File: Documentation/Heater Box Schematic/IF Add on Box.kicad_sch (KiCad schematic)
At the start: 21 parts, among them J1 DB37 Female, J2 DB37 Male, K1 Heater Relay, M1 Fan

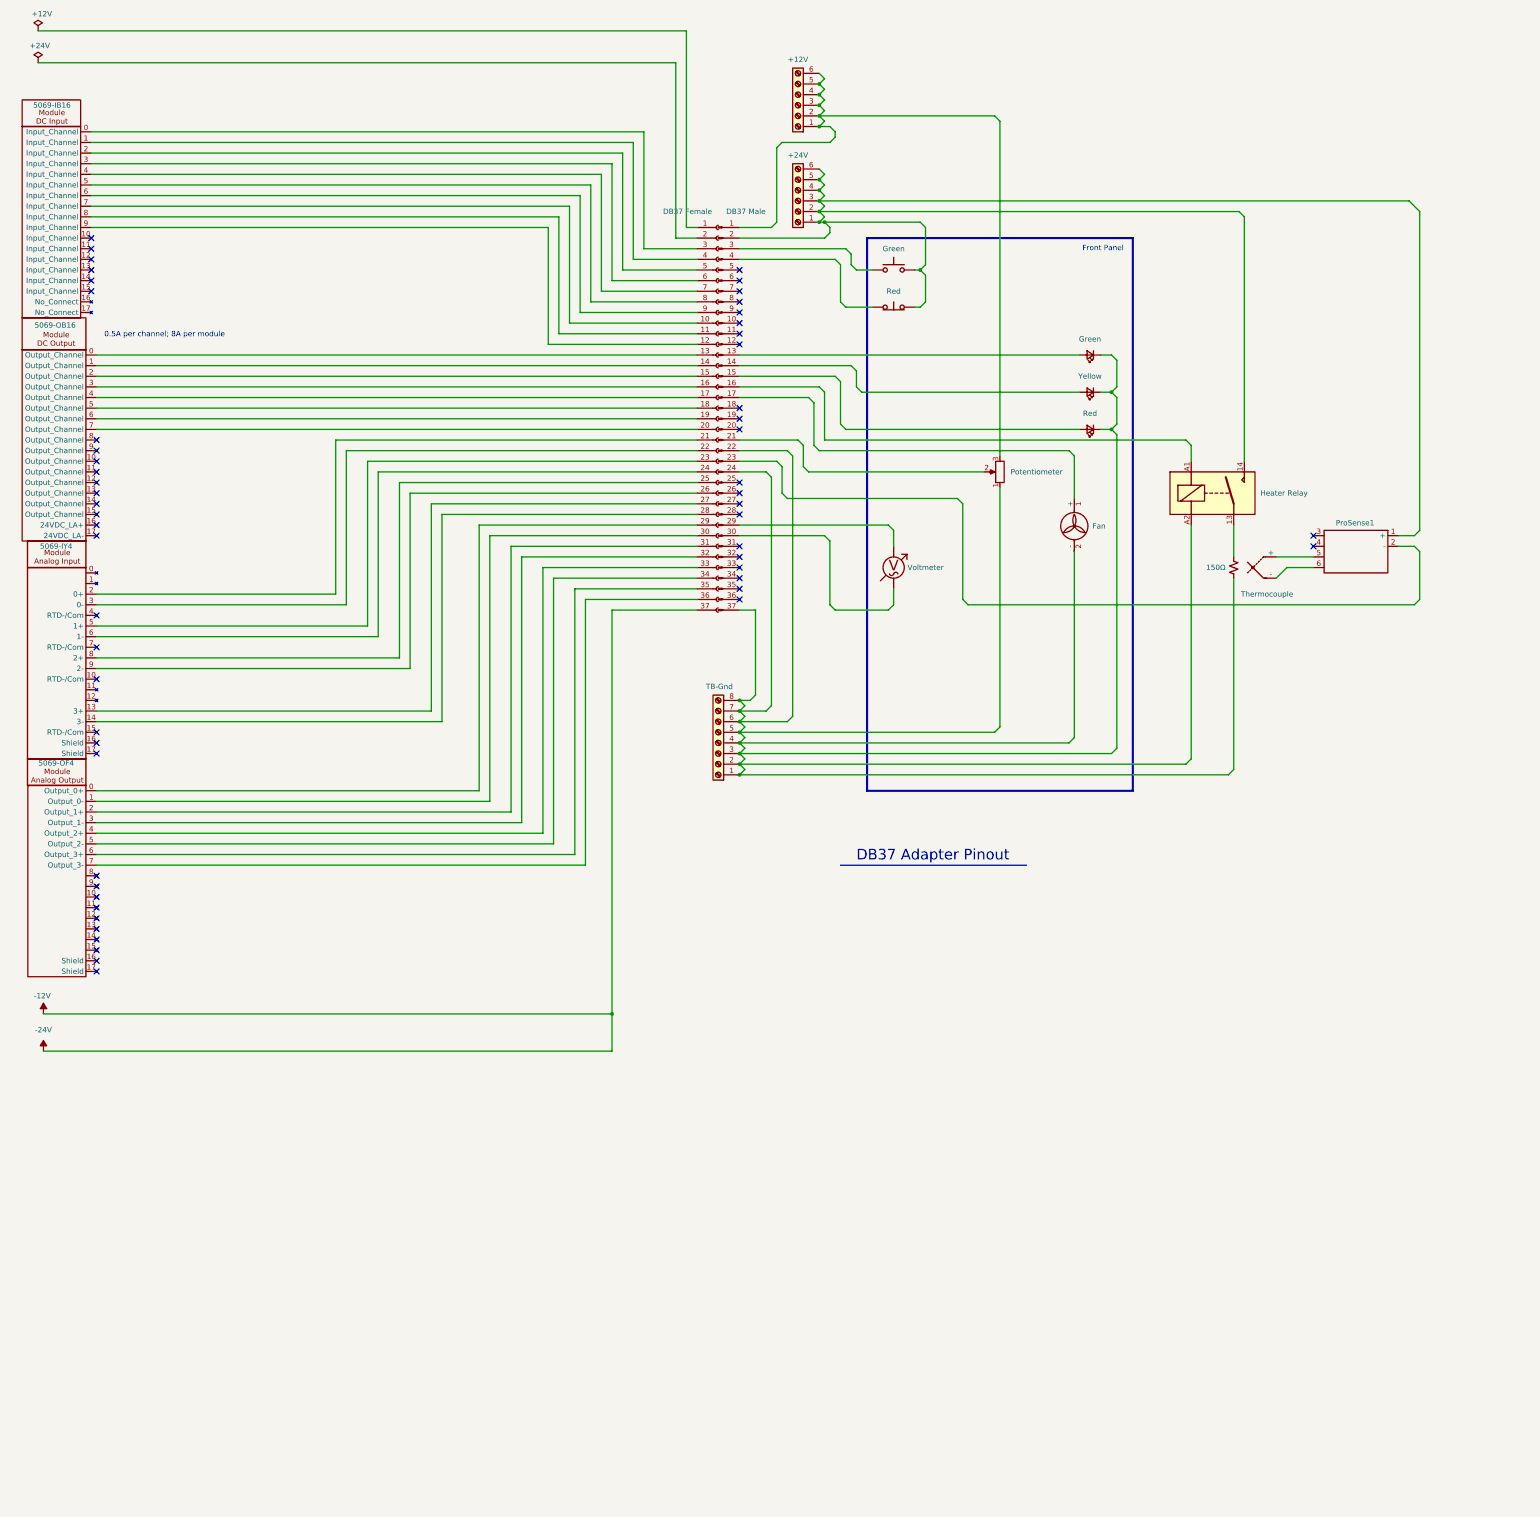
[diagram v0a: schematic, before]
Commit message: Add per-module heater box schematics and update LaTeX figures
Split the single heater box schematic into four sub-sheets (Din, Dout,
Ain, Aout) in KiCad and replace the overview figure in the LaTeX paper
with individual figures for each I/O module with descriptive captions.

Co-Authored-By: Claude Opus 4.6 (1M context) <noreply@anthropic.com>
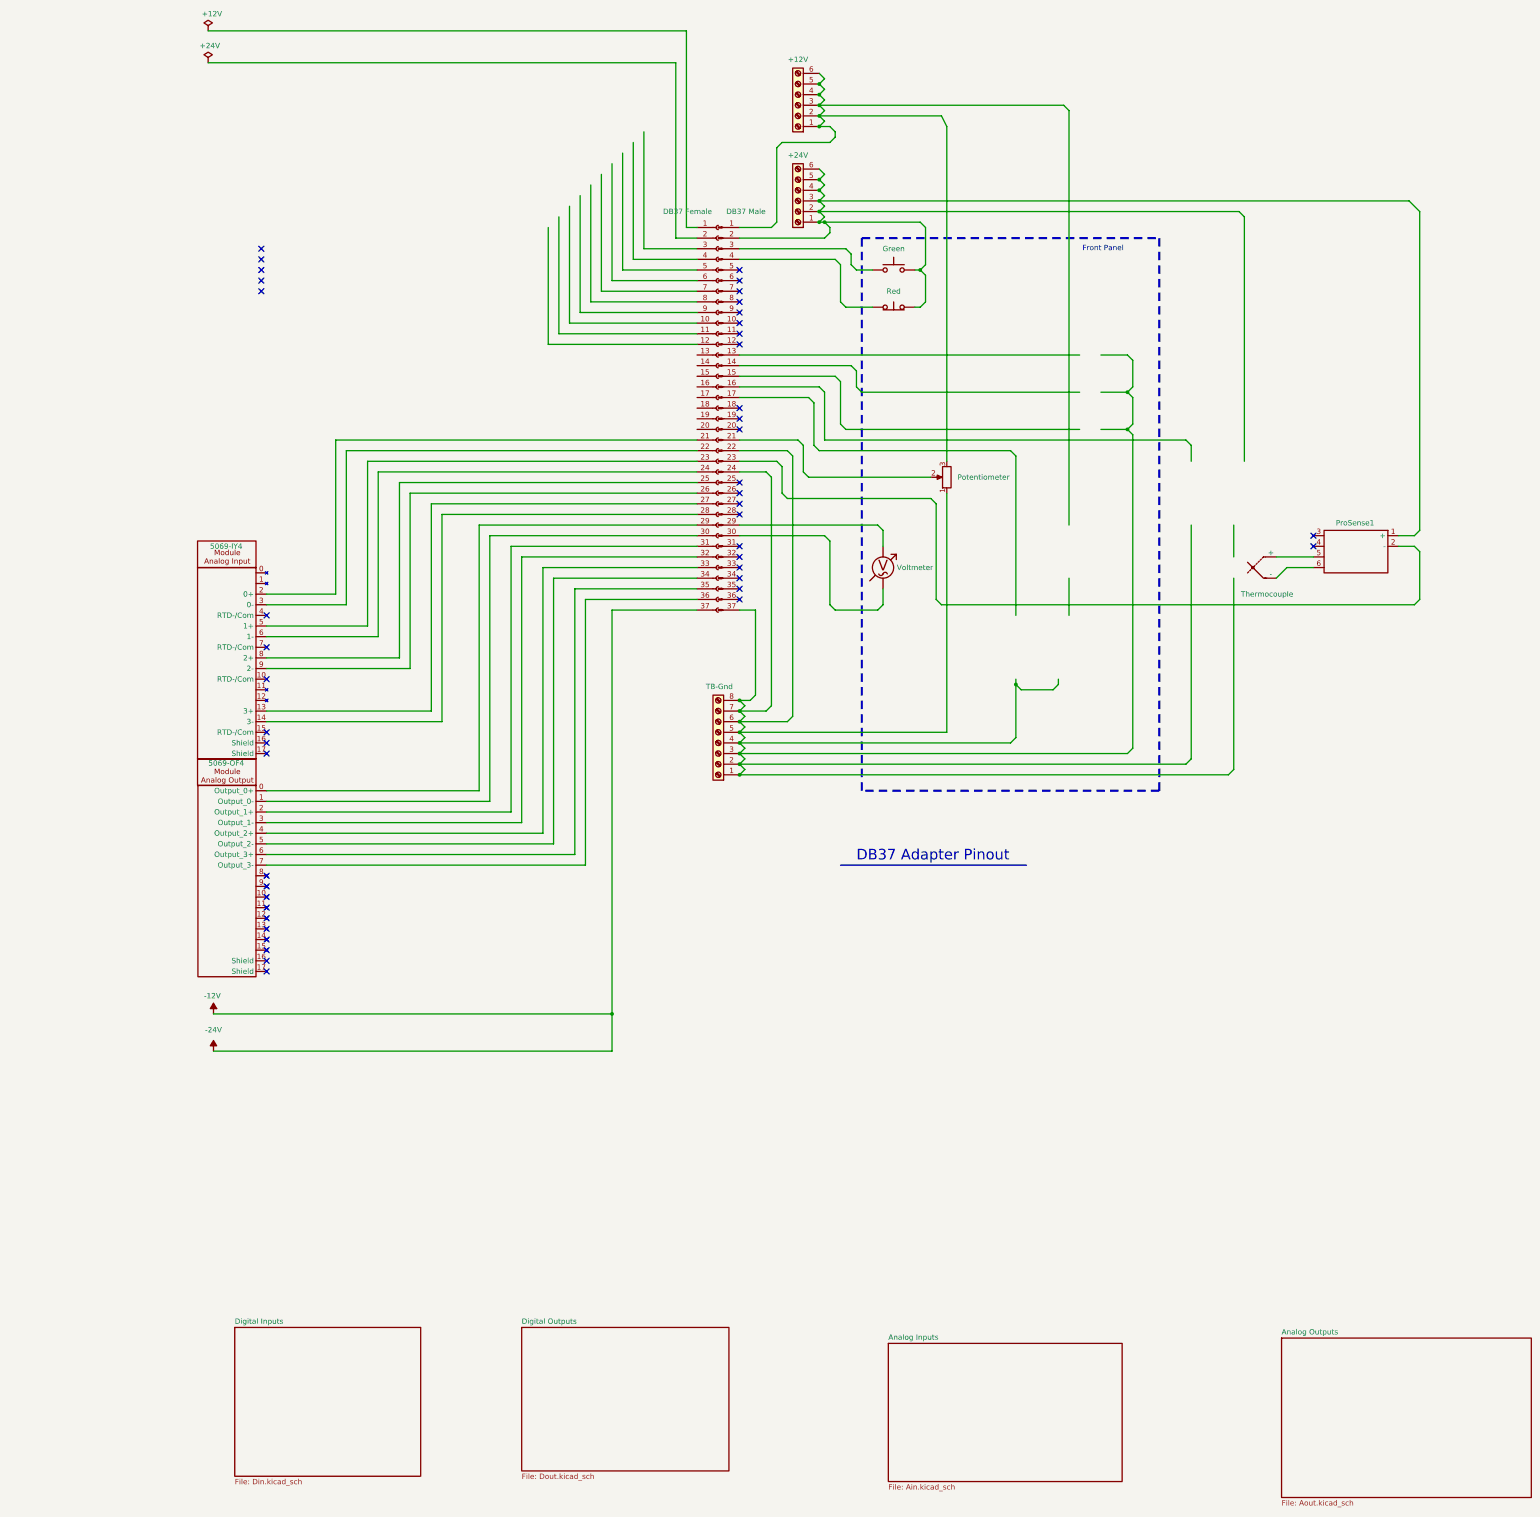
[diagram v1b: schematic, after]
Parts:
- removed 5069-IB16: ~, symbol PLC5380I-Ocards:5069 IB16 DC Input
- removed 5069-OB16: ~, symbol PLC5380I-Ocards:5069 OB16 DC Output
- removed Green, Red, Yellow: LED_Small, symbol Device:LED_Small
- removed K1: Heater Relay, symbol Relay:Relay_SPST-NO
- removed M1: Fan, symbol Motor:Fan
- removed R1: 150Ω, symbol Device:R_Small_US
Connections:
- no-connect marks 55 -> 44
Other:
- added sheet Analog Inputs (Ain.kicad_sch)
- added sheet Analog Outputs (Aout.kicad_sch)
- added sheet Digital Inputs (Din.kicad_sch)
- added sheet Digital Outputs (Dout.kicad_sch)
- note removed: "0.5A per channel; 8A per module"
- company: (none) -> ISU
- title: (none) -> Heater Process Box
- moved on the sheet: 5069-IY4, 5069-OF4, Potentiometer
